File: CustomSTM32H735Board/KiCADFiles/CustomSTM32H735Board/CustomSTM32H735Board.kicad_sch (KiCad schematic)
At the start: 12 parts, among them U1 STM32H735IGKx, U2 STM32H735IGTx

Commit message: started to assign LCD connector to STM32H735. Added NRST and Boot0 switch.
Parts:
- removed U1: STM32H735IGKx, Package_BGA:UFBGA-201_10x10mm_Layout15x15_P0.65mm, symbol MCU_ST_STM32H7:STM32H735IGKx
- removed U2: STM32H735IGTx, Package_QFP:LQFP-176_24x24mm_P0.5mm, symbol MCU_ST_STM32H7:STM32H735IGTx
- added C5, C?: 100nF, symbol Device:C
- added C?: PGB1010603, PGB1010603:ESD_PGB1010603MR, symbol Private:PGB1010603
- added J1: FLE-125-01-G-DV, Private:CON50_2X25_UF_FLE_SAI, symbol Private:FLE-125-01-G-DV
- added R3: 10k, symbol Device:R
- added SW1, SW2: SW_Wuerth_450301014042, Button_Switch_THT:SW_Slide-03_Wuerth-WS-SLTV_10x2.5x6.4_P2.54mm, symbol Switch:SW_Wuerth_450301014042
- added SW?: SW_Omron_B3FS, symbol Switch:SW_Omron_B3FS
- added U1: STM32H735IGT6, Private:LQFP176_STM32H735IGT6_STM-M, symbol Private:STM32H735IGT6
- added X1: NSC5004A-25M, Private:NSC5004_NDK, symbol Private:NSC5004A-25M
- renumbered C5 to C6, C6 to C7
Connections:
- net +3.3V: now also C2.1, C4.1, C7.1, UHYPERRAM1.B4 (VCC), UHYPERRAM1.D1 (VCCQ), UHYPERRAM1.E4 (VCCQ), R3.1, X1.4 (VCC)
- net GND: now also C5.1, C?.1, C?.2, SW?.1, X1.2 (GND)
- net NRST: now also C?.1, C?.2, SW?.2, U1.33
- net PB2: now also UFLASH1.B2 (SCLK), U1.57 (PB2-OCTOSPIM_P1_CLK); no longer UFLASH1.C3 (DQS)
- net PE2: now also U1.1 (PE2-OCTOSPIM_P1_IO2)
- net PF0: now also U1.18 (PF0-OCTOSPIM_P2_IO0)
- net PF1: now also U1.19 (PF1-OCTOSPIM_P2_IO1)
- net PF10: now also J1.22, U1.30 (PF10-LTDC_DE); no longer UFLASH1.B2 (SCLK)
- net PF12: now also U1.59 (PF12-OCTOSPIM_P2_DQS)
- net PF2: now also U1.20 (PF2-OCTOSPIM_P2_IO2)
- net PF3: now also U1.21 (PF3-OCTOSPIM_P2_IO3)
- net PF4: now also U1.22 (PF4-OCTOSPIM_P2_CLK)
- net PG0: now also U1.63 (PG0-OCTOSPIM_P2_IO4)
- net PG1: now also U1.66 (PG1-OCTOSPIM_P2_IO5)
- net PG10: now also U1.154 (PG10-OCTOSPIM_P2_IO6)
- net PG11: now also U1.155 (PG11-OCTOSPIM_P2_IO7)
- net PG12: now also U1.156 (PG12-OCTOSPIM_P2_NCS)
- net PG6: now also U1.116 (PG6-OCTOSPIM_P1_NCS)
- net PD11 renamed PF8
- net PF8: now also U1.28 (PF8-OCTOSPIM_P1_IO0)
- net PD12 renamed PF9
- net PF9: now also U1.29 (PF9-OCTOSPIM_P1_IO1)
- net PD13 renamed PA6
- net PA6: now also U1.51 (PA6-OCTOSPIM_P1_IO3)
- net PD4 renamed PE7
- net PE7: now also U1.67 (PE7-OCTOSPIM_P1_IO4)
- net PD5 renamed PC2_C
- net PC2_C: now also U1.36 (PC2_C-OCTOSPIM_P1_IO5)
- net PD7 renamed PE10
- net PE10: now also U1.72 (PE10-OCTOSPIM_P1_IO7)
- net PG9 renamed PC3_C
- net PC3_C: now also U1.37 (PC3_C-OCTOSPIM_P1_IO6)
- new net: C5.2, R3.2, X1.1 (STAND-BY)
- new net: SW1.1 (B), U1.40
- new net BOOT0: U1.167
- new net PA1: J1.7, U1.42 (PA1-LTDC_R2)
- new net PA10: J1.23, U1.129 (PA10-LTDC_B1)
- new net PA11: J1.11, U1.130 (PA11-LTDC_R4)
- new net PA15: J1.33, U1.139 (PA15(JTDI)-LTDC_B6)
- new net PA2: J1.5, U1.43 (PA2-LTDC_R1)
- new net PA3: J1.31, U1.46 (PA3-LTDC_B5)
- new net PA7: J1.28
- new net PA9: J1.13, U1.128 (PA9-LTDC_R5)
- new net PB0: J1.9
- new net PB1: J1.15
- new net PB15: J1.18, U1.88 (PB15-LTDC_G7)
- new net PC0: J1.8, U1.34 (PC0-LTDC_G2)
- new net PC1: J1.14, U1.35 (PC1-LTDC_G5)
- new net PC4: J1.17
- new net PC5: U1.54 (PC5-OCTOSPIM_P1_DQS), UFLASH1.C3 (DQS)
- new net PC6: J1.26, U1.122 (PC6-LTDC_HSYNC)
- new net PC9: J1.25, U1.125 (PC9-LTDC_B2)
- new net PD10: J1.27, U1.91 (PD10-LTDC_B3)
- new net PD2: J1.35, U1.145 (PD2-LTDC_B7)
- new net PE11: J1.10, U1.73 (PE11-LTDC_G3)
- new net PE12: J1.29, U1.74 (PE12-LTDC_B4)
- new net PE14: J1.30, U1.76 (PE14-LTDC_CLK)
- new net PE4: J1.21, U1.3 (PE4-LTDC_B0)
- new net PE5: J1.4, U1.4 (PE5-LTDC_G0)
- new net PE6: J1.6, U1.5 (PE6-LTDC_G1)
- new net PF14: J1.40, U1.61 (PF14-I2C4_SCL)
- new net PF15: J1.38, U1.62 (PF15-I2C4_SDA)
- new net PG13: J1.3, U1.157 (PG13-LTDC_R0)
- new net PG15: J1.43
- new net PG2: J1.39
- new net PG3: J1.24
- new net PH0: U1.31 (PH0-OSC_IN-RCC_OSC_IN), X1.3 (OUTPUT)
- new net PJ11: J1.12
- new net PK1: J1.16, U1.108 (PK1-LTDC_G6)
- new net VDD: SW1.2 (C), U1.105, U1.113, U1.126, U1.13, U1.136, U1.152, U1.160, U1.176, U1.25, U1.44, U1.48, U1.65, U1.7, U1.71, U1.84, U1.92, U1.99
- new net VSS: U1.100, U1.106, U1.112, U1.119, U1.12, U1.134, U1.137, U1.151, U1.159, U1.173, U1.24, U1.45, U1.47, U1.6, U1.70, U1.81, U1.83, U1.93
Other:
- moved on the sheet: R1

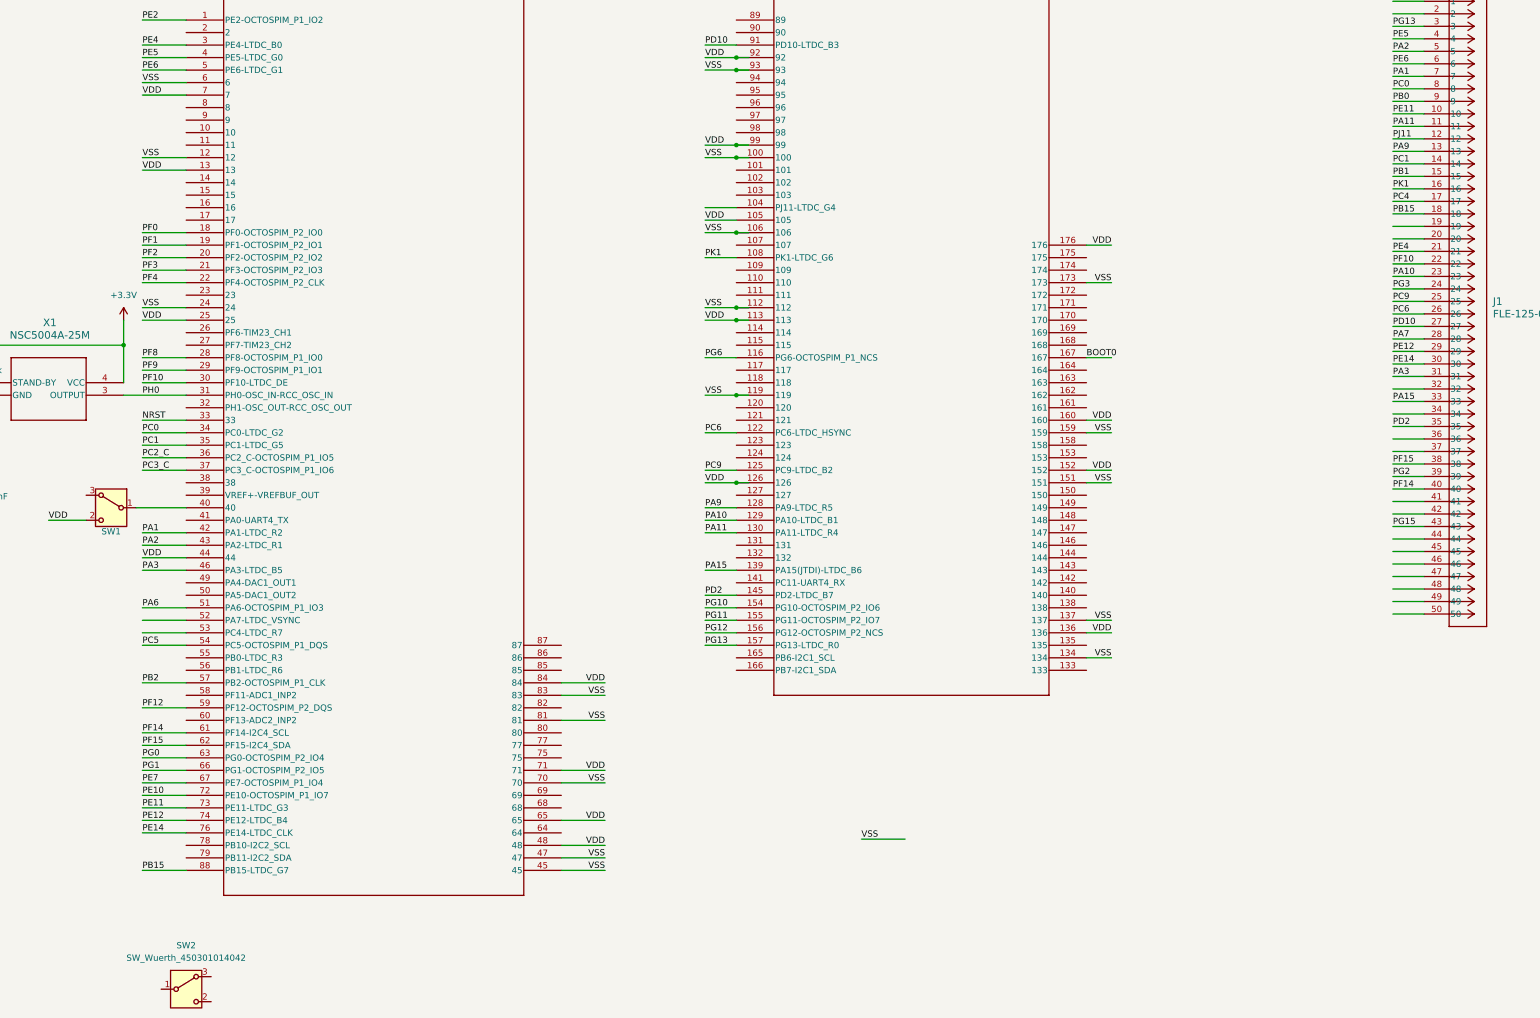
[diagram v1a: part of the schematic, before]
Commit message: added VSS and VDD on custom board layout
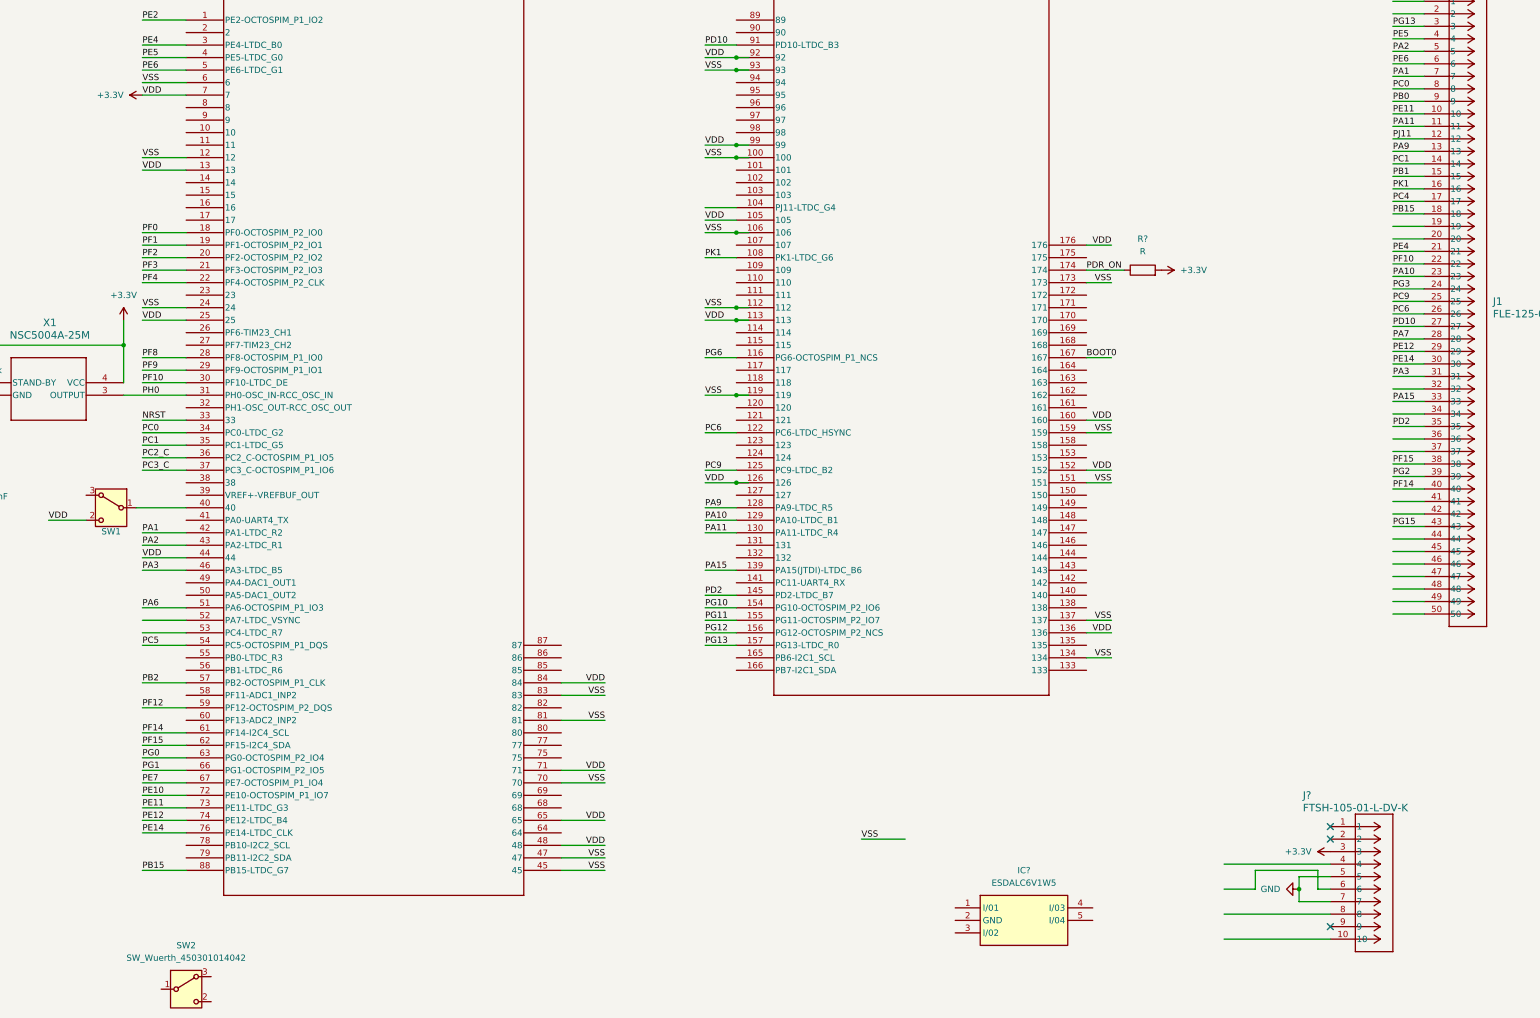
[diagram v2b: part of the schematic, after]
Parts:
- added IC?: ESDALC6V1W5, Private:SOT65P210X110-5N, symbol Private:ESDALC6V1W5
- added J?: FTSH-105-01-L-DV-K, Private:CON10_2X5_DUK_FTSH_SAI-M, symbol Private:FTSH-105-01-L-DV-K
- added R?: R, symbol Device:R
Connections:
- net VDD is gone; now on net +3.3V: SW1.2 (C), U1.105, U1.113, U1.126, U1.13, U1.136, U1.152, U1.160, U1.176, U1.25, U1.44, U1.48, U1.65, U1.7, U1.71, U1.84, U1.92, U1.99
- net +3.3V: now also J?.3, R?.2
- net GND: now also J?.5, J?.7
- net PDR_ON: now reaches U1.174
- net PDR_ON: now also R?.1
- no-connect marks 7 -> 10

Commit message: cleaned up repo by eliminating double STM32-DK files
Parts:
- removed SW2: SW_Wuerth_450301014042, Button_Switch_THT:SW_Slide-03_Wuerth-WS-SLTV_10x2.5x6.4_P2.54mm, symbol Switch:SW_Wuerth_450301014042
- added C10, C11, C12: 2.2uF low ESR, symbol Device:C
- added L1: L, symbol Device:L
- added R5, R6, R7: 22R, symbol Device:R
- gave numbers to parts that had none: 6
- renumbered C1 to C2, C2 to C4, C3 to C5, C4 to C6, C5 to C7, C6 to C8, C7 to C9, J1 to J2, SW1 to SW2
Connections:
- net +3.3V: now also J1.1, U1.135, U1.175, U1.8, U1.82; no longer J1.3
- net GND: now also J1.3, C10.1, C11.2, C12.1; no longer J1.7
- net NRST: now also R7.1
- net PA7: now also U1.52 (PA7-LTDC_VSYNC)
- net PB0: now also U1.55 (PB0-LTDC_R3)
- net PB1: now also U1.56 (PB1-LTDC_R6)
- net PC4: now also U1.53 (PC4-LTDC_R7)
- net PJ11: now also U1.104 (PJ11-LTDC_G4)
- net VSS: now also U1.121, U1.14, U1.16, U1.17, U1.38, U1.64
- net PF6: now reaches U1.26 (PF6-TIM23_CH1)
- net PF7: now reaches U1.27 (PF7-TIM23_CH2)
- net at U1.39 (VREF+-VREFBUF_OUT): now also SW2.3 (A)
- net at SW2.1 (B): now also L1.1; no longer U1.40
- net PA0: now reaches U1.41 (PA0-UART4_TX)
- net PA4: now reaches U1.49 (PA4-DAC1_OUT1)
- net PA5: now reaches U1.50 (PA5-DAC1_OUT2)
- net PF11: now reaches U1.58 (PF11-ADC1_INP2)
- net PF13: now reaches U1.60 (PF13-ADC2_INP2)
- net PB10: now reaches U1.78 (PB10-I2C2_SCL)
- net PB11: now reaches U1.79 (PB11-I2C2_SDA)
- net at U1.80: now also C10.2
- net at J1.10: now also R7.2
- net at J1.2: now also R5.2
- net at J1.4: now also R6.2
- net PA13: now reaches U1.132
- net PA13: now also R5.1
- net at U1.133: now also C11.1
- net PA14: now reaches U1.138
- net PA14: now also R6.1
- net PC11: now reaches U1.141 (PC11-UART4_RX)
- net PB6: now reaches U1.165 (PB6-I2C1_SCL)
- net PB7: now reaches U1.166 (PB7-I2C1_SDA)
- net at U1.172: now also C12.2
- new net: L1.2, U1.40
- no-connect marks 10 -> 13
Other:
- moved on the sheet: SW2

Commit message: Work on layout and PCB of custom board. All connectors added. PCB size first draft.
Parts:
- removed IC1: ESDALC6V1W5, Private:SOT65P210X110-5N, symbol Private:ESDALC6V1W5
- removed SW2: SW_Wuerth_450301014042, Button_Switch_THT:SW_Slide-03_Wuerth-WS-SLTV_10x2.5x6.4_P2.54mm, symbol Switch:SW_Wuerth_450301014042
- added C10, C11: 10uF, Capacitor_SMD:C_0805_2012Metric_Pad1.18x1.45mm_HandSolder, symbol Device:C
- added C12: 220pF, Capacitor_SMD:C_0805_2012Metric_Pad1.18x1.45mm_HandSolder, symbol Device:C
- added FB1: FBMJ1608, Inductor_SMD:L_0603_1608Metric_Pad1.05x0.95mm_HandSolder, symbol Device:FerriteBead
- added FB2: FCM1608, Inductor_SMD:L_0603_1608Metric_Pad1.05x0.95mm_HandSolder, symbol Device:FerriteBead
- added H1, H2, H3, H4, H5, H6, H7, H8: MountingHole_Pad_MP, MountingHole:MountingHole_2.7mm_M2.5_Pad_TopBottom, symbol Mechanical:MountingHole_Pad_MP
- added J1: Conn_01x03_Socket, Connector_JST:JST_XH_B2B-XH-AM_1x02_P2.50mm_Vertical, symbol Connector:Conn_01x03_Socket
- added J2: Conn_02x10_Odd_Even, Connector_IDC:IDC-Header_2x10_P2.54mm_Vertical, symbol Connector_Generic:Conn_02x10_Odd_Even
- added JADC1: Conn_01x02_Socket, Connector_JST:JST_XH_B3B-XH-A_1x03_P2.50mm_Vertical, symbol Connector:Conn_01x02_Socket
- added JDAC1, JI2C1, JI2C2, JI2C3, JUART1: Conn_01x03_Socket, Connector_JST:JST_XH_B3B-XH-A_1x03_P2.50mm_Vertical, symbol Connector:Conn_01x03_Socket
- added JP1: SolderJumper_3_Open, Jumper:SolderJumper-3_P1.3mm_Open_Pad1.0x1.5mm_NumberLabels, symbol Jumper:SolderJumper_3_Open
- added R10: 5k1, Resistor_SMD:R_0805_2012Metric_Pad1.20x1.40mm_HandSolder, symbol Device:R
- added R4, R5, R6, R7, R8, R9: 4.7k, Resistor_SMD:R_0805_2012Metric_Pad1.20x1.40mm_HandSolder, symbol Device:R
- added TP1: TestPoint, Connector_Pin:Pin_D0.7mm_L6.5mm_W1.8mm_FlatFork, symbol Connector:TestPoint
- C13: renamed from C10; value 2.2uF low ESR -> 4.7uF low ESR; footprint (none) -> Capacitor_SMD:C_0805_2012Metric_Pad1.18x1.45mm_HandSolder
- C14: renamed from C11; value 2.2uF low ESR -> 4.7uF low ESR; footprint (none) -> Capacitor_SMD:C_0805_2012Metric_Pad1.18x1.45mm_HandSolder
- C15: renamed from C12; value 2.2uF low ESR -> 4.7uF low ESR; footprint (none) -> Capacitor_SMD:C_0805_2012Metric_Pad1.18x1.45mm_HandSolder
- C2, C3, C4, C5, C9: footprint (none) -> Capacitor_SMD:C_0805_2012Metric_Pad1.18x1.45mm_HandSolder
- C6: renamed from C8; footprint (none) -> Capacitor_SMD:C_0805_2012Metric_Pad1.18x1.45mm_HandSolder
- C7: renamed from C6; footprint (none) -> Capacitor_SMD:C_0805_2012Metric_Pad1.18x1.45mm_HandSolder
- C8: renamed from C7; footprint (none) -> Capacitor_SMD:C_0805_2012Metric_Pad1.18x1.45mm_HandSolder
- L1: value L -> 2.2uH; footprint (none) -> Inductor_SMD:L_Murata_DFE201610P
- R1, R2, R3: footprint (none) -> Resistor_SMD:R_0805_2012Metric_Pad1.20x1.40mm_HandSolder
- R11: renamed from R4; footprint (none) -> Resistor_SMD:R_0805_2012Metric_Pad1.20x1.40mm_HandSolder
- R12: renamed from R5; footprint (none) -> Resistor_SMD:R_0805_2012Metric_Pad1.20x1.40mm_HandSolder
- R13: renamed from R6; footprint (none) -> Resistor_SMD:R_0805_2012Metric_Pad1.20x1.40mm_HandSolder
- R14: renamed from R7; footprint (none) -> Resistor_SMD:R_0805_2012Metric_Pad1.20x1.40mm_HandSolder
- SW1: footprint (none) -> Button_Switch_SMD:SW_SPST_Omron_B3FS-100xP
- renumbered J1 to J3, J2 to J4
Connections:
- net +3.3V: now also FB1.1, J1.2 (Pin_2), JP1.1 (A), R4.2, R5.2, R6.2, R7.2, R8.2, R9.2; no longer U1.135, U1.175, U1.82
- net BOOT0: now also R10.1
- net GND: now also U1.100, U1.106, U1.112, U1.119, U1.12, U1.121, U1.134, U1.137, U1.151, U1.159, U1.173, U1.24, U1.38, U1.45, U1.47, U1.6, U1.64, U1.70, U1.81, U1.83, U1.93, C10.2, C11.2, C12.1, J1.1 (Pin_1), J2.1 (Pin_1), J2.2 (Pin_2), JADC1.1 (Pin_1), JDAC1.1 (Pin_1), JI2C1.1 (Pin_1), JI2C2.1 (Pin_1), JI2C3.1 (Pin_1), JUART1.1 (Pin_1), R10.2
- net PC2_C: now also JADC1.2 (Pin_2)
- net VDD_SDC: now reaches C13.2, U1.80
- net VDD_SDC: now also C14.1, C15.2, L1.1, U1.133, U1.135, U1.17, U1.172, U1.175, U1.82, C11.1, TP1.1
- net at U1.40: now also FB2.2; no longer L1.2
- net VLXSMPS: now reaches U1.15
- net VLXSMPS: now also L1.2, C12.2
- net at U1.39 (VREF+-VREFBUF_OUT): now also JP1.3 (B)
- net PA8: now reaches U1.127
- removed net VSS: U1.100, U1.106, U1.112, U1.119, U1.12, U1.121, U1.134, U1.137, U1.14, U1.151, U1.159, U1.16, U1.17, U1.173, U1.24, U1.38, U1.45, U1.47, U1.6, U1.64, U1.70, U1.81, U1.83, U1.93
- new net: FB2.1, JP1.2 (C)
- new net +5V: J1.3 (Pin_3)
- new net ADC1: J2.19 (Pin_19)
- new net ADC2: J2.20 (Pin_20)
- new net DAC1: JDAC1.2 (Pin_2)
- new net DAC2: JDAC1.3 (Pin_3)
- new net LSBUSB: J2.11 (Pin_11), J2.12 (Pin_12)
- new net RXTX: J2.3 (Pin_3), J2.4 (Pin_4), J2.5 (Pin_5), J2.6 (Pin_6)
- new net R_CH1: J2.17 (Pin_17)
- new net R_CH2: J2.18 (Pin_18)
- new net S0: J2.13 (Pin_13), J2.14 (Pin_14)
- new net S1: J2.15 (Pin_15), J2.16 (Pin_16)
- new net SCL1: JI2C3.3 (Pin_3), R9.1
- new net SCL2: JI2C2.3 (Pin_3), R8.1
- new net SCL4: JI2C1.3 (Pin_3), R7.1
- new net SDA1: JI2C3.2 (Pin_2), R6.1
- new net SDA2: JI2C2.2 (Pin_2), R5.1
- new net SDA4: JI2C1.2 (Pin_2), R4.1
- new net UART_RX: JUART1.2 (Pin_2)
- new net UART_TX: JUART1.3 (Pin_3)
- new net VDDSMPS: C10.1, FB1.2, U1.16
- new net VSSSMPS: U1.14
- new net nRXTX: J2.10 (Pin_10), J2.7 (Pin_7), J2.8 (Pin_8), J2.9 (Pin_9)
- no-connect marks 13 -> 12
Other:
- moved on the sheet: C5, C6
